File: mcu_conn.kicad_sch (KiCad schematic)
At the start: 42 parts, among them J11 MD_MCU_PU_EN, J9 MD_MCU_EN, Q6 FDV305N, U2 Teensy4.1, U3 INA190A5IDDFR, U4 INA190A5IDDFR

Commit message: Schematic freeze: add C10, probe headers, buffer link and Teensy taps
SCHEMATIC FROZEN at this commit. 164 parts, 108 nets, ERC 0 errors.
All remaining work is layout. Do not change the schematic without
telling the group.

Top sheet:
- C10 (10u) back between VOUT_LDO and the J6 SMA
- J18 VIN_PROBE, J19 VREF_PROBE, J20 VOUT_PROBE: 2-pin headers with
  pin 1 on VDD_LDO, NR, VOUT_LDO and pin 2 on GND
- IBIAS and NR labels changed from local to global

Buffer sheet:
- R40 (0 ohm) in series between R34 and VDD_LDO

MCU sheet:
- J21 to J25, VG0_PROBE to VG4_PROBE: 2-pin headers with pin 1 on
  VG0 to VG4 and pin 2 on GND
- R51, R52, R53 (0 ohm, DNP) from Teensy pins 23, 22, 21 to MD,
  IBIAS, NR
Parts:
- added J21: VG0_PROBE, ldo_bringup_board_ee372:CONN_PxC02S_SUL, symbol ldo_bringup_board_ee372:PEC02SAAN
- added J22: VG1_PROBE, ldo_bringup_board_ee372:CONN_PxC02S_SUL, symbol ldo_bringup_board_ee372:PEC02SAAN
- added J23: VG2_PROBE, ldo_bringup_board_ee372:CONN_PxC02S_SUL, symbol ldo_bringup_board_ee372:PEC02SAAN
- added J24: VG3_PROBE, ldo_bringup_board_ee372:CONN_PxC02S_SUL, symbol ldo_bringup_board_ee372:PEC02SAAN
- added J25: VG4_PROBE, ldo_bringup_board_ee372:CONN_PxC02S_SUL, symbol ldo_bringup_board_ee372:PEC02SAAN
- added R51, R52, R53: 0, Resistor_SMD:R_0603_1608Metric_Pad0.98x0.95mm_HandSolder, symbol Device:R
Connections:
- net GND: now also J21.2, J22.2, J23.2, J24.2, J25.2
- net MD: now also R51.2
- net VG0: now also J21.1
- net VG1: now also J22.1
- net VG2: now also J23.1
- net VG3: now also J24.1
- net VG4: now also J25.1
- net at U2.43 (21_A7_RX5_BCLK1): now also R53.1
- net at U2.44 (22_A8_CTX1): now also R52.1
- net at U2.45 (23_A9_CRX1_MCLK1): now also R51.1
- new net IBIAS: R52.2
- new net NR: R53.2
- no-connect marks 28 -> 25
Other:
- moved on the sheet: R22, R23, R24, R25, R26, TP15, TP16, TP17, TP18, TP19

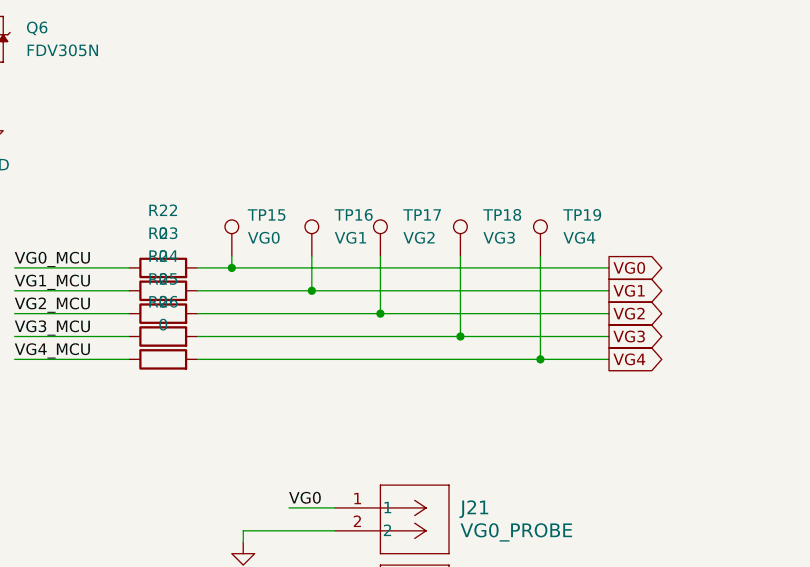
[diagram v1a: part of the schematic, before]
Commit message: Schematic changes after the freeze: drop 14 test points, add R54, move input caps
The schematic changed after the freeze commit f5ce739. It now has 151
parts and 109 nets. ERC 0 errors.

- Removed TP9 to TP13 and TP15 to TP19 (on VG0 to VG4) and TP22 to TP25
  (on the four shunt nodes)
- Added R54 (0 ohm, 0805, DNP) between the J3 IBIAS jack and the IBIAS
  net at U1 pin 5
- C6, C7, C9 and C11 moved from VDD (SHUNT_IN_A) to VDD_LDO
  (SHUNT_IN_B), the chip side of the R4 shunt
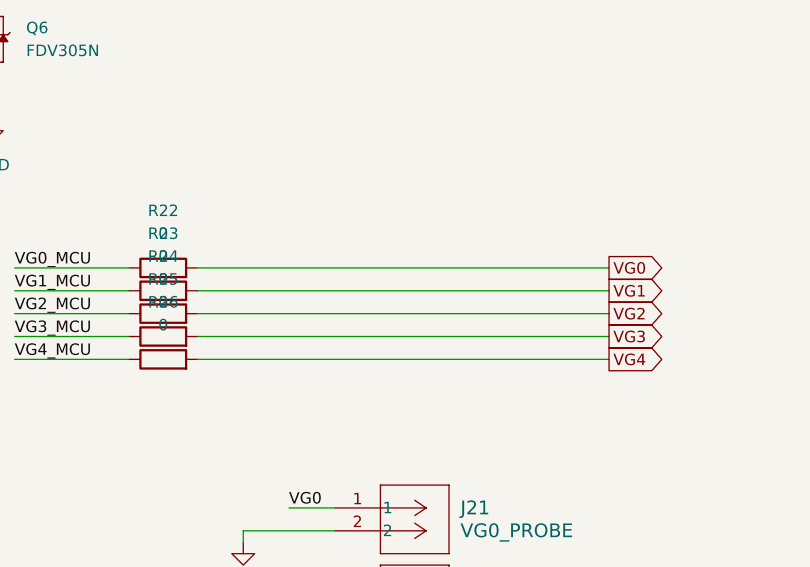
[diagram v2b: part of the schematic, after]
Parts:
- removed TP15: VG0, TestPoint:TestPoint_Keystone_5005-5009_Compact, symbol Connector:TestPoint
- removed TP16: VG1, TestPoint:TestPoint_Keystone_5005-5009_Compact, symbol Connector:TestPoint
- removed TP17: VG2, TestPoint:TestPoint_Keystone_5005-5009_Compact, symbol Connector:TestPoint
- removed TP18: VG3, TestPoint:TestPoint_Keystone_5005-5009_Compact, symbol Connector:TestPoint
- removed TP19: VG4, TestPoint:TestPoint_Keystone_5005-5009_Compact, symbol Connector:TestPoint

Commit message: Add bring-up notes to the schematic
Text notes only, no parts or nets change. Leave R3, R21, R29 to R32,
R40, R44 and R55 off at first. Possibly lift C6 and C11 when driving
VIN from the buffer. Add a large pull-down on the buffer input.
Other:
- note added: "Initially leave off R29"
- note added: "Initially leave off R30"
- note added: "Initially leave off R31"
- note added: "Initially leave off R32"
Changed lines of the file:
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@@
+		)
+	)
+	(text "Initially leave off R29"
+		(exclude_from_sim yes)
+		(at 23.876 167.64 0)
+		(effects
+			(font
+				(size 1.27 1.27)
+			)
+			(justify left)
 		)
 	)
@@
 		)
 	)
+	(text "Initially leave off R32"
+		(exclude_from_sim yes)
+		(at 23.114 145.288 0)
+		(effects
+			(font
+				(size 1.27 1.27)
+			)
+			(justify left)
+		)
+	)
+	(text "Initially leave off R30"
+		(exclude_from_sim yes)
+		(at 24.384 188.468 0)
+		(effects
+			(font
+				(size 1.27 1.27)
+			)
+			(justify left)
+		)
+	)
+	(text "Initially leave off R31"
+		(exclude_from_sim yes)
+		(at 23.622 127.508 0)
+		(effects
+			(font
+				(size 1.27 1.27)
+			)
+			(justify left)
+		)
+	)
